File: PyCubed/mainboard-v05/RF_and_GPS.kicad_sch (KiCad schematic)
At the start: 22 parts, among them J5 Amphenol_901-144, J6 Amphenol_901-144, J7 Amphenol_901-144, U13 EP2W+, U14 S1216V8, U23 RFM98PW, U9 TPS54226PWPRPWP14_2P31X2P46-L

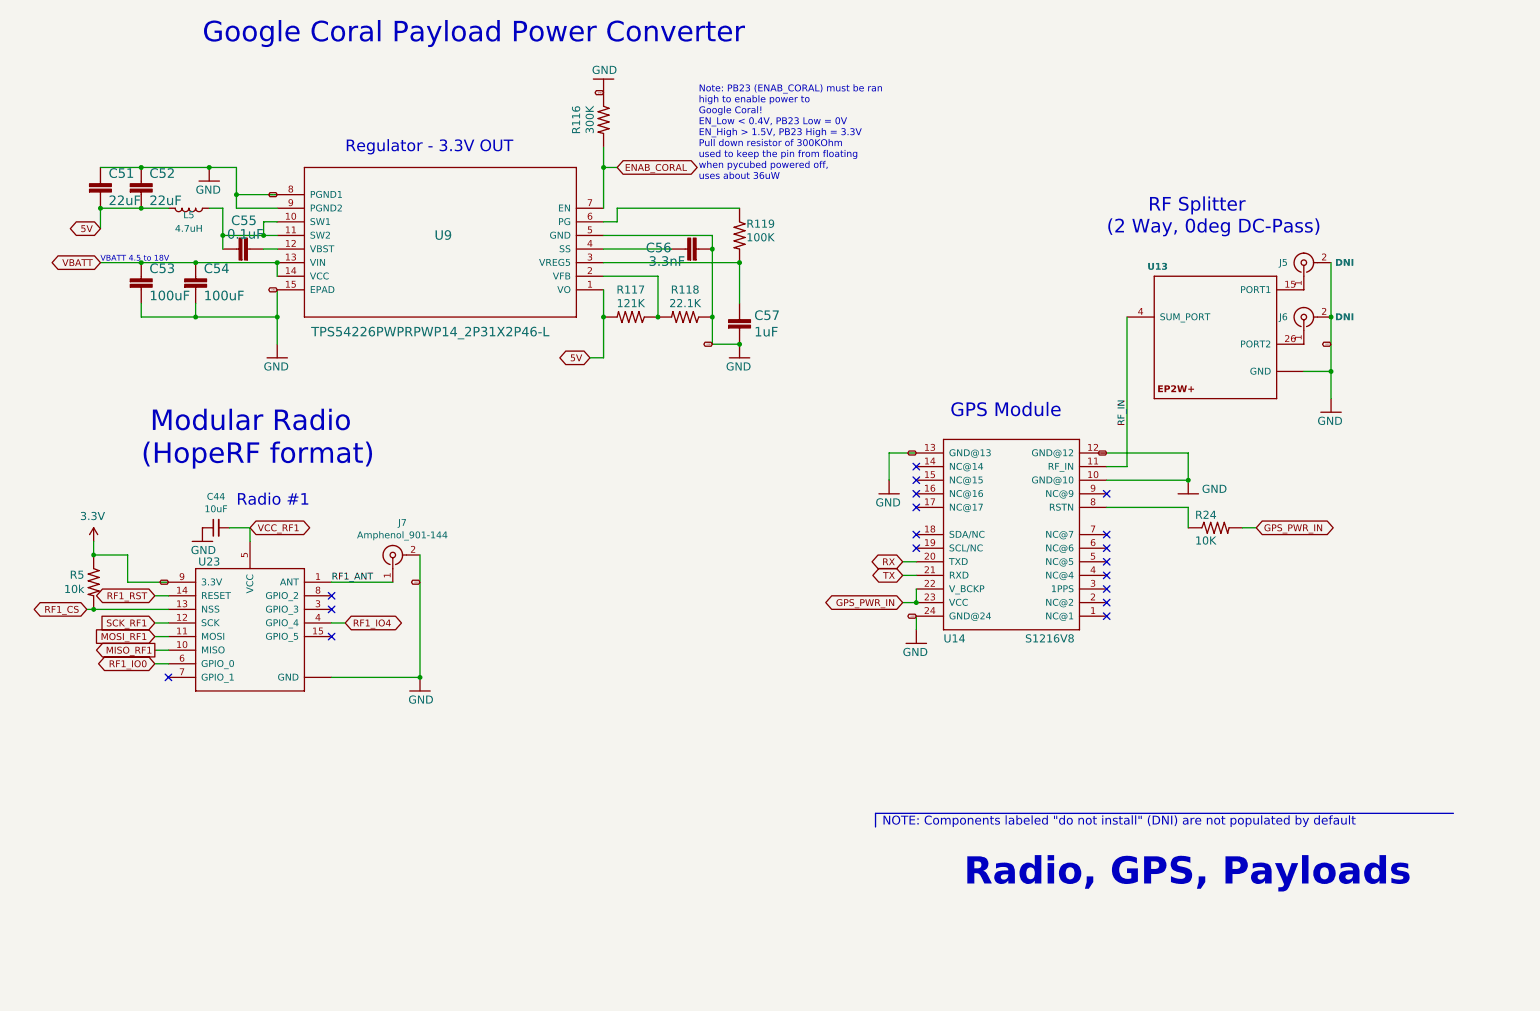
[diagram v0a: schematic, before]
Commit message: add replacement sensors
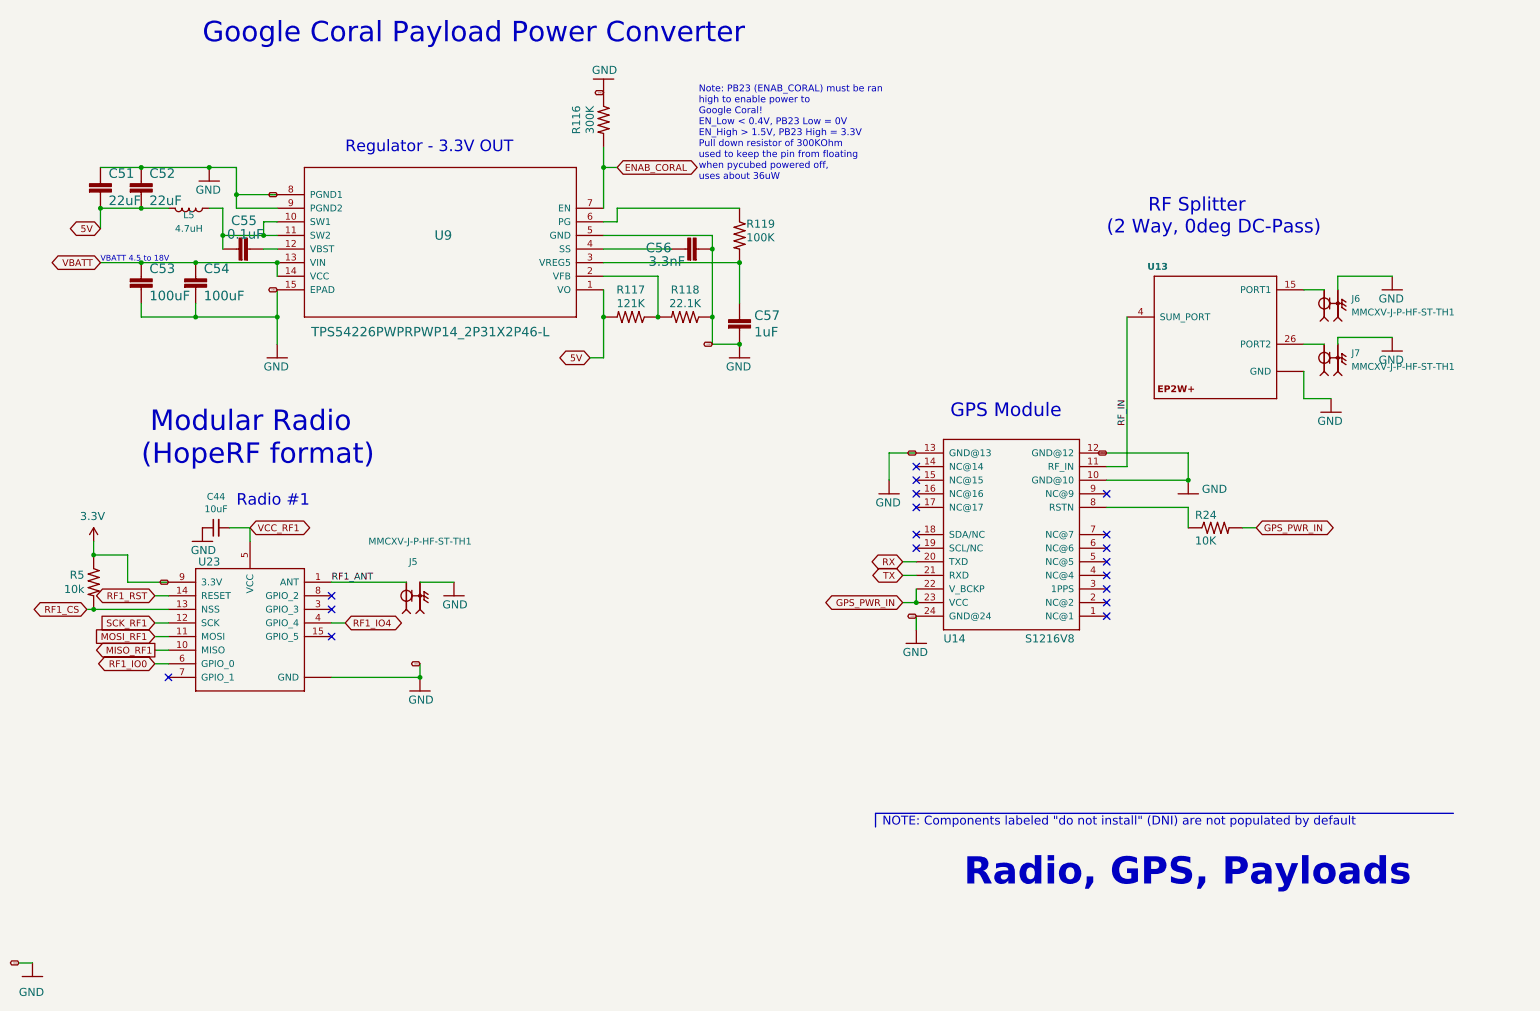
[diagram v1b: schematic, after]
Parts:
- removed J5, J6, J7: Amphenol_901-144, mainboard:SMA_901-144-horizontal, symbol Connector:Conn_Coaxial
- added J5: MMCXV-J-P-HF-ST-TH1, mainboard:SAMTEC_MMCXV-J-P-HF-ST-TH1, symbol mainboard:MMCXV-J-P-HF-ST-TH1
- added J6, J7: MMCXV-J-P-HF-ST-TH1, SAMTEC_MMCXV-J-P-HF-ST-TH1, symbol mainboard:MMCXV-J-P-HF-ST-TH1
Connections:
- net GND: now also J5.S1, J5.S2, J5.S3, J5.S4, J6.S1, J6.S2, J6.S3, J6.S4, J7.S1, J7.S2, J7.S3, J7.S4
- net RF1_ANT: now also J5.1
- net at U13.15 (PORT1): now also J6.1
- net at U13.26 (PORT2): now also J7.1
